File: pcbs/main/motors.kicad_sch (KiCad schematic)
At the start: 49 parts, among them J2 Jumpers, Q1 2SC945, Q2 2SC945, Q3 2SC945, Q4 2SC945, Q5 2SC945, Q6 2SC945, Q7 2SC945, Q8 2SC945

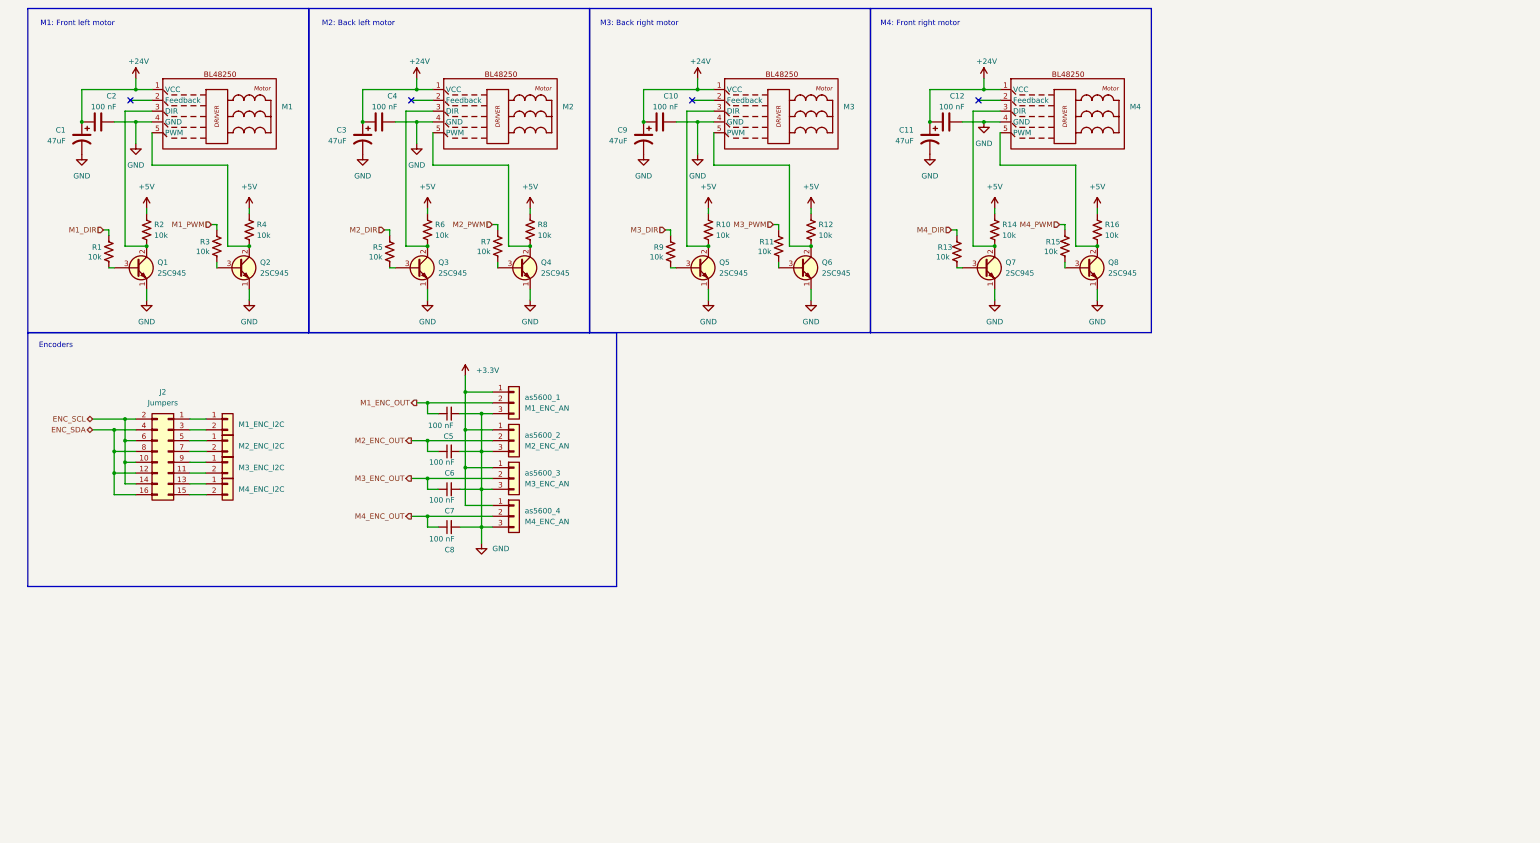
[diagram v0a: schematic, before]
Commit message: Add circuit for motor feedback
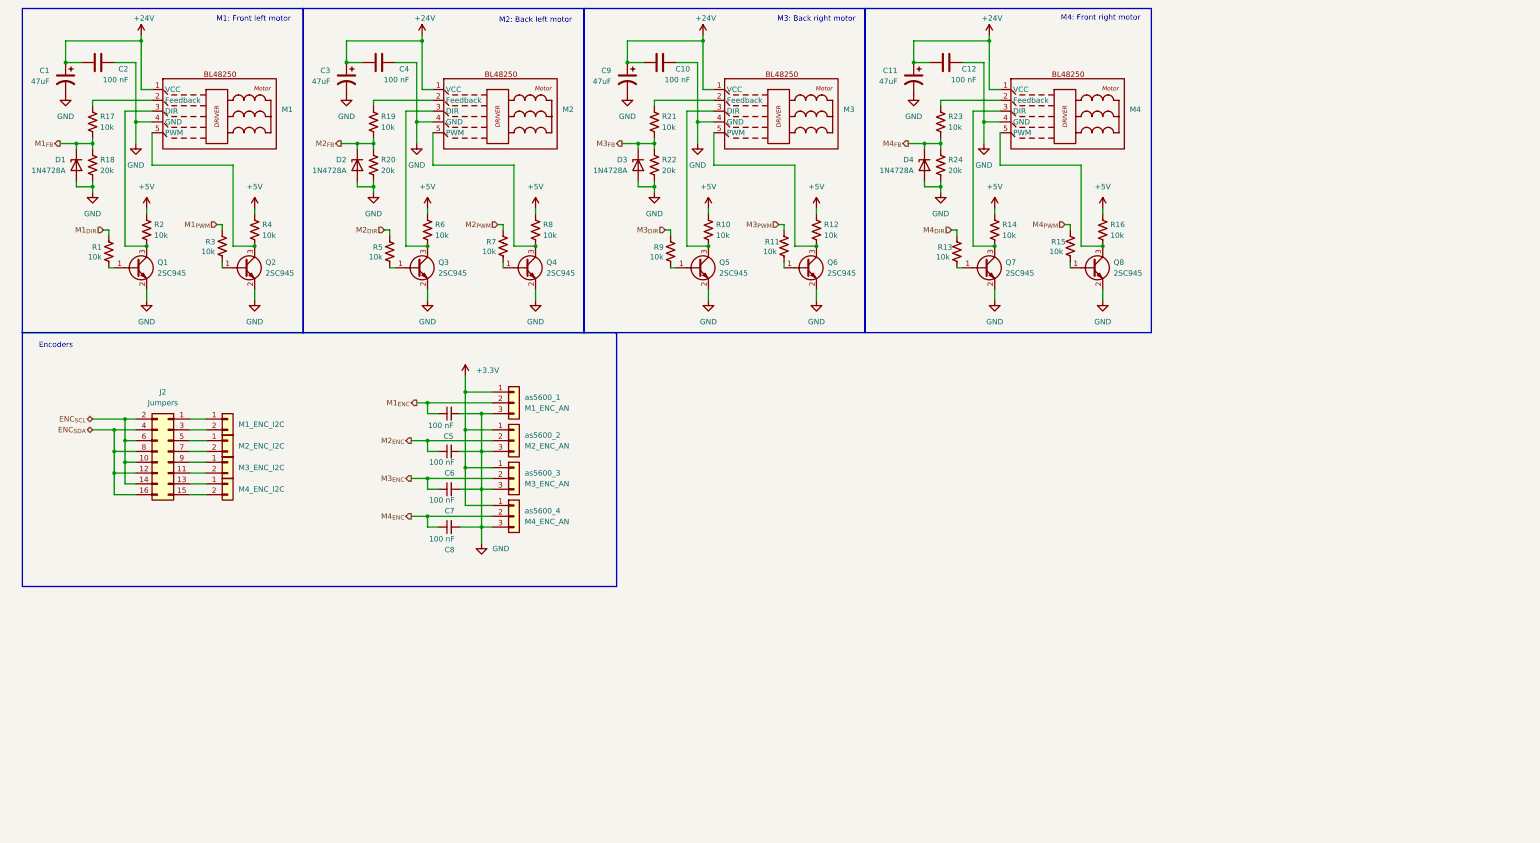
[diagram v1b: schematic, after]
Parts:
- added D1, D2, D3, D4: 1N4728A, Diode_THT:D_DO-41_SOD81_P10.16mm_Horizontal, symbol Diode:1N47xxA
- added R17, R19, R21, R23: 10k, Resistor_THT:R_Axial_DIN0207_L6.3mm_D2.5mm_P7.62mm_Horizontal, symbol Device:R_US
- added R18, R20, R22, R24: 20k, Resistor_THT:R_Axial_DIN0207_L6.3mm_D2.5mm_P7.62mm_Horizontal, symbol Device:R_US
- M1, M2, M3, M4: symbol BL48250:BL48250 -> oxebots:BL48250
- Q1, Q2, Q3, Q4, Q5, Q6, Q7, Q8: footprint Package_TO_SOT_THT:TO-92L_Inline_Wide -> Package_TO_SOT_THT:TO-220-3_Vertical; symbol PCM_Transistor_BJT_AKL:2SC945 -> Transistor_BJT:2SC1945
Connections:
- net GND: now also Q1.2 (E), Q2.2 (E), Q3.2 (E), Q4.2 (E), Q5.2 (E), Q6.2 (E), Q7.2 (E), Q8.2 (E), D1.2 (A), D2.2 (A), D3.2 (A), D4.2 (A), R18.1, R20.1, R22.1, R24.1; no longer Q1.1 (E), Q2.1 (E), Q3.1 (E), Q4.1 (E), Q5.1 (E), Q6.1 (E), Q7.1 (E), Q8.1 (E)
- net at M3.3 (DIR), R10.1: now also Q5.3 (C); no longer Q5.2 (C)
- net at M1.5 (PWM), R4.1: now also Q2.3 (C); no longer Q2.2 (C)
- net at R3.2: now also Q2.1 (B); no longer Q2.3 (B)
- net at M1.3 (DIR), R2.1: now also Q1.3 (C); no longer Q1.2 (C)
- net at R15.2: now also Q8.1 (B); no longer Q8.3 (B)
- net at M2.2 (Feedback): now also R19.2
- net at M2.3 (DIR), R6.1: now also Q3.3 (C); no longer Q3.2 (C)
- net at M2.5 (PWM), R8.1: now also Q4.3 (C); no longer Q4.2 (C)
- net at R13.2: now also Q7.1 (B); no longer Q7.3 (B)
- net at R5.2: now also Q3.1 (B); no longer Q3.3 (B)
- net at R9.2: now also Q5.1 (B); no longer Q5.3 (B)
- net at R11.2: now also Q6.1 (B); no longer Q6.3 (B)
- net at M4.5 (PWM), R16.1: now also Q8.3 (C); no longer Q8.2 (C)
- net at M3.2 (Feedback): now also R21.2
- net at M3.5 (PWM), R12.1: now also Q6.3 (C); no longer Q6.2 (C)
- net at R7.2: now also Q4.1 (B); no longer Q4.3 (B)
- net at M4.3 (DIR), R14.1: now also Q7.3 (C); no longer Q7.2 (C)
- net at M4.2 (Feedback): now also R23.2
- net at R1.2: now also Q1.1 (B); no longer Q1.3 (B)
- net at M1.2 (Feedback): now also R17.2
- net ENC_SCL renamed ENC_{SCL}
- net ENC_SDA renamed ENC_{SDA}
- net M1_DIR renamed M1_{DIR}
- net M1_ENC_OUT renamed M1_{ENC}
- net M1_PWM renamed M1_{PWM}
- net M2_DIR renamed M2_{DIR}
- net M2_ENC_OUT renamed M2_{ENC}
- net M2_PWM renamed M2_{PWM}
- net M3_DIR renamed M3_{DIR}
- net M3_ENC_OUT renamed M3_{ENC}
- net M3_PWM renamed M3_{PWM}
- net M4_DIR renamed M4_{DIR}
- net M4_ENC_OUT renamed M4_{ENC}
- net M4_PWM renamed M4_{PWM}
- new net M1_{FB}: D1.1 (K), R17.1, R18.2
- new net M2_{FB}: D2.1 (K), R19.1, R20.2
- new net M3_{FB}: D3.1 (K), R21.1, R22.2
- new net M4_{FB}: D4.1 (K), R23.1, R24.2
- no-connect marks 4 -> 0
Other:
- moved on the sheet: C1, C2, Q2, Q4, Q6, Q8, R11, R12, R15, R16, R3, R4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

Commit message: Add some probes & update footprints
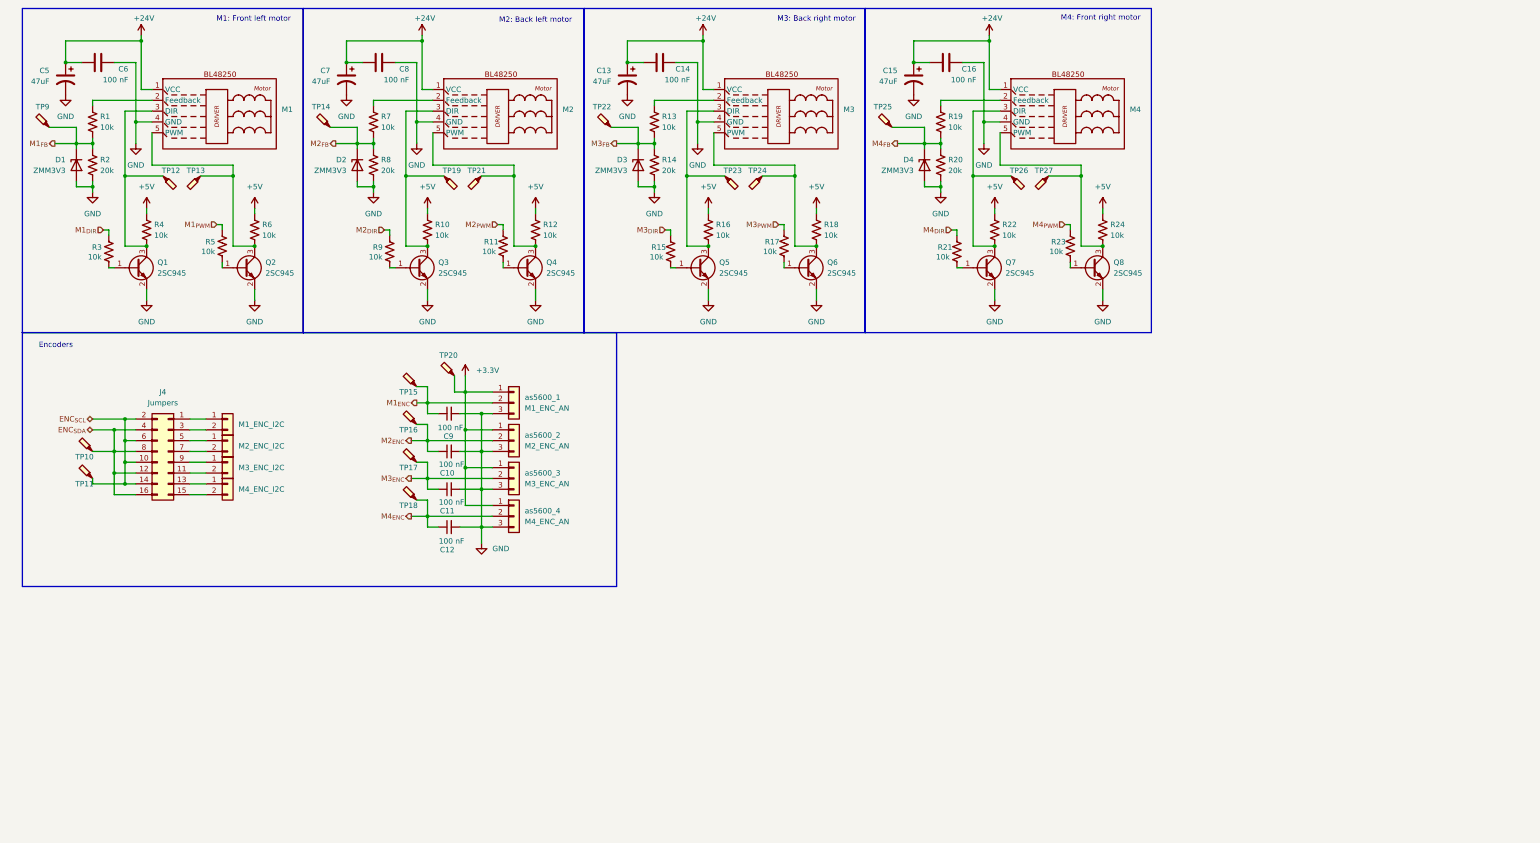
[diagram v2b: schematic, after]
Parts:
- added TP10, TP11, TP17, TP18, TP19, TP21, TP22, TP24, TP25, TP26, TP27: TestPoint_Probe, TestPoint:TestPoint_Pad_D1.0mm, symbol Connector:TestPoint_Probe
- added TP12, TP13, TP14, TP15, TP16, TP20, TP23, TP9: TestPoint_Probe, TestPoint:TestPoint_Loop_D2.50mm_Drill1.0mm_LowProfile, symbol Connector:TestPoint_Probe
- C10: renamed from C6; footprint Capacitor_THT:C_Disc_D5.0mm_W2.5mm_P2.50mm -> Capacitor_SMD:C_0603_1608Metric
- C11: renamed from C7; footprint Capacitor_THT:C_Disc_D5.0mm_W2.5mm_P2.50mm -> Capacitor_SMD:C_0603_1608Metric
- C12: renamed from C8; footprint Capacitor_THT:C_Disc_D5.0mm_W2.5mm_P2.50mm -> Capacitor_SMD:C_0603_1608Metric
- C14: renamed from C10; footprint Capacitor_THT:C_Disc_D5.0mm_W2.5mm_P2.50mm -> Capacitor_SMD:C_0603_1608Metric
- C16: renamed from C12; footprint Capacitor_THT:C_Disc_D5.0mm_W2.5mm_P2.50mm -> Capacitor_SMD:C_0603_1608Metric
- C6: renamed from C2; footprint Capacitor_THT:C_Disc_D5.0mm_W2.5mm_P2.50mm -> Capacitor_SMD:C_0603_1608Metric
- C8: renamed from C4; footprint Capacitor_THT:C_Disc_D5.0mm_W2.5mm_P2.50mm -> Capacitor_SMD:C_0603_1608Metric
- C9: renamed from C5; footprint Capacitor_THT:C_Disc_D5.0mm_W2.5mm_P2.50mm -> Capacitor_SMD:C_0603_1608Metric
- D1, D2, D3, D4: value 1N4728A -> ZMM3V3; footprint Diode_THT:D_DO-41_SOD81_P10.16mm_Horizontal -> Diode_SMD:D_MiniMELF; symbol Diode:1N47xxA -> Diode:ZMMxx
- Q1, Q2, Q3, Q4, Q5, Q6, Q7, Q8: footprint Package_TO_SOT_THT:TO-220-3_Vertical -> Package_TO_SOT_THT:TO-92; symbol Transistor_BJT:2SC1945 -> oxebots:2SC945
- R1: renamed from R17; footprint Resistor_THT:R_Axial_DIN0207_L6.3mm_D2.5mm_P7.62mm_Horizontal -> Resistor_SMD:R_0603_1608Metric
- R10: renamed from R6; footprint Resistor_THT:R_Axial_DIN0207_L6.3mm_D2.5mm_P7.62mm_Horizontal -> Resistor_SMD:R_0603_1608Metric
- R11: renamed from R7; footprint Resistor_THT:R_Axial_DIN0207_L6.3mm_D2.5mm_P7.62mm_Horizontal -> Resistor_SMD:R_0603_1608Metric
- R12: renamed from R8; footprint Resistor_THT:R_Axial_DIN0207_L6.3mm_D2.5mm_P7.62mm_Horizontal -> Resistor_SMD:R_0603_1608Metric
- R13: renamed from R21; footprint Resistor_THT:R_Axial_DIN0207_L6.3mm_D2.5mm_P7.62mm_Horizontal -> Resistor_SMD:R_0603_1608Metric
- R14: renamed from R22; footprint Resistor_THT:R_Axial_DIN0207_L6.3mm_D2.5mm_P7.62mm_Horizontal -> Resistor_SMD:R_0603_1608Metric
- R15: renamed from R9; footprint Resistor_THT:R_Axial_DIN0207_L6.3mm_D2.5mm_P7.62mm_Horizontal -> Resistor_SMD:R_0603_1608Metric
- R16: renamed from R10; footprint Resistor_THT:R_Axial_DIN0207_L6.3mm_D2.5mm_P7.62mm_Horizontal -> Resistor_SMD:R_0603_1608Metric
- R17: renamed from R11; footprint Resistor_THT:R_Axial_DIN0207_L6.3mm_D2.5mm_P7.62mm_Horizontal -> Resistor_SMD:R_0603_1608Metric
- R18: renamed from R12; footprint Resistor_THT:R_Axial_DIN0207_L6.3mm_D2.5mm_P7.62mm_Horizontal -> Resistor_SMD:R_0603_1608Metric
- R19: renamed from R23; footprint Resistor_THT:R_Axial_DIN0207_L6.3mm_D2.5mm_P7.62mm_Horizontal -> Resistor_SMD:R_0603_1608Metric
- R2: renamed from R18; footprint Resistor_THT:R_Axial_DIN0207_L6.3mm_D2.5mm_P7.62mm_Horizontal -> Resistor_SMD:R_0603_1608Metric
- R20: renamed from R24; footprint Resistor_THT:R_Axial_DIN0207_L6.3mm_D2.5mm_P7.62mm_Horizontal -> Resistor_SMD:R_0603_1608Metric
- R21: renamed from R13; footprint Resistor_THT:R_Axial_DIN0207_L6.3mm_D2.5mm_P7.62mm_Horizontal -> Resistor_SMD:R_0603_1608Metric
- R22: renamed from R14; footprint Resistor_THT:R_Axial_DIN0207_L6.3mm_D2.5mm_P7.62mm_Horizontal -> Resistor_SMD:R_0603_1608Metric
- R23: renamed from R15; footprint Resistor_THT:R_Axial_DIN0207_L6.3mm_D2.5mm_P7.62mm_Horizontal -> Resistor_SMD:R_0603_1608Metric
- R24: renamed from R16; footprint Resistor_THT:R_Axial_DIN0207_L6.3mm_D2.5mm_P7.62mm_Horizontal -> Resistor_SMD:R_0603_1608Metric
- R3: renamed from R1; footprint Resistor_THT:R_Axial_DIN0207_L6.3mm_D2.5mm_P7.62mm_Horizontal -> Resistor_SMD:R_0603_1608Metric
- R4: renamed from R2; footprint Resistor_THT:R_Axial_DIN0207_L6.3mm_D2.5mm_P7.62mm_Horizontal -> Resistor_SMD:R_0603_1608Metric
- R5: renamed from R3; footprint Resistor_THT:R_Axial_DIN0207_L6.3mm_D2.5mm_P7.62mm_Horizontal -> Resistor_SMD:R_0603_1608Metric
- R6: renamed from R4; footprint Resistor_THT:R_Axial_DIN0207_L6.3mm_D2.5mm_P7.62mm_Horizontal -> Resistor_SMD:R_0603_1608Metric
- R7: renamed from R19; footprint Resistor_THT:R_Axial_DIN0207_L6.3mm_D2.5mm_P7.62mm_Horizontal -> Resistor_SMD:R_0603_1608Metric
- R8: renamed from R20; footprint Resistor_THT:R_Axial_DIN0207_L6.3mm_D2.5mm_P7.62mm_Horizontal -> Resistor_SMD:R_0603_1608Metric
- R9: renamed from R5; footprint Resistor_THT:R_Axial_DIN0207_L6.3mm_D2.5mm_P7.62mm_Horizontal -> Resistor_SMD:R_0603_1608Metric
- renumbered C9 to C13, C11 to C15, C1 to C5, C3 to C7, J2 to J4
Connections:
- net +3.3V: now also TP20.1
- net ENC_{SCL}: now also TP11.1
- net ENC_{SDA}: now also TP10.1
- net M1_{ENC}: now also TP15.1
- net M1_{FB}: now also TP9.1
- net M2_{ENC}: now also TP16.1
- net M2_{FB}: now also TP14.1
- net M3_{ENC}: now also TP17.1
- net M3_{FB}: now also TP22.1
- net M4_{ENC}: now also TP18.1
- net M4_{FB}: now also TP25.1
- net at M3.3 (DIR), Q5.3 (C), R16.1: now also TP23.1
- net at M1.5 (PWM), Q2.3 (C), R6.1: now also TP13.1
- net at M1.3 (DIR), Q1.3 (C), R4.1: now also TP12.1
- net at M2.3 (DIR), Q3.3 (C), R10.1: now also TP19.1
- net at M2.5 (PWM), Q4.3 (C), R12.1: now also TP21.1
- net at M4.5 (PWM), Q8.3 (C), R24.1: now also TP27.1
- net at M3.5 (PWM), Q6.3 (C), R18.1: now also TP24.1
- net at M4.3 (DIR), Q7.3 (C), R22.1: now also TP26.1

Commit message: Add NRF24 pwr adapter as standalone components
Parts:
- M1: value (none) -> FRONT_LEFT_MOTOR
- M2: value (none) -> BACK_LEFT_MOTOR
- M3: value (none) -> BACK_RIGHT_MOTOR
- M4: value (none) -> FRONT_RIGHT_MOTOR
- TP10: renamed from TP12; value TestPoint_Probe -> M1_DIR_Probe; footprint TestPoint:TestPoint_Loop_D2.50mm_Drill1.0mm_LowProfile -> TestPoint:TestPoint_Pad_D1.0mm
- TP11: renamed from TP13; value TestPoint_Probe -> M1_PWM_Probe
- TP12: renamed from TP14; value TestPoint_Probe -> M2_FB_Probe
- TP13: renamed from TP15; value TestPoint_Probe -> M1_ENC_Probe
- TP14: renamed from TP16; value TestPoint_Probe -> M2_ENC_Probe
- TP15: renamed from TP17; value TestPoint_Probe -> M3_ENC_Probe; footprint TestPoint:TestPoint_Pad_D1.0mm -> TestPoint:TestPoint_Loop_D2.50mm_Drill1.0mm_LowProfile
- TP16: renamed from TP18; value TestPoint_Probe -> M4_ENC_Probe; footprint TestPoint:TestPoint_Pad_D1.0mm -> TestPoint:TestPoint_Loop_D2.50mm_Drill1.0mm_LowProfile
- TP17: renamed from TP19; value TestPoint_Probe -> M2_DIR_Probe
- TP18: renamed from TP20; value TestPoint_Probe -> ENC_VCC_Probe; footprint TestPoint:TestPoint_Loop_D2.50mm_Drill1.0mm_LowProfile -> TestPoint:TestPoint_Pad_D1.0mm
- TP19: renamed from TP21; value TestPoint_Probe -> M2_PWM_Probe; footprint TestPoint:TestPoint_Pad_D1.0mm -> TestPoint:TestPoint_Loop_D2.50mm_Drill1.0mm_LowProfile
- TP20: renamed from TP22; value TestPoint_Probe -> M3_FB_Probe; footprint TestPoint:TestPoint_Pad_D1.0mm -> TestPoint:TestPoint_Loop_D2.50mm_Drill1.0mm_LowProfile
- TP21: renamed from TP23; value TestPoint_Probe -> M3_DIR_Probe; footprint TestPoint:TestPoint_Loop_D2.50mm_Drill1.0mm_LowProfile -> TestPoint:TestPoint_Pad_D1.0mm
- TP22: renamed from TP24; value TestPoint_Probe -> M3_PWM_Probe; footprint TestPoint:TestPoint_Pad_D1.0mm -> TestPoint:TestPoint_Loop_D2.50mm_Drill1.0mm_LowProfile
- TP23: renamed from TP25; value TestPoint_Probe -> M4_FB_Probe; footprint TestPoint:TestPoint_Pad_D1.0mm -> TestPoint:TestPoint_Loop_D2.50mm_Drill1.0mm_LowProfile
- TP24: renamed from TP26; value TestPoint_Probe -> M4_DIR_Probe
- TP25: renamed from TP27; value TestPoint_Probe -> M4_PWM_Probe; footprint TestPoint:TestPoint_Pad_D1.0mm -> TestPoint:TestPoint_Loop_D2.50mm_Drill1.0mm_LowProfile
- TP7: renamed from TP9; value TestPoint_Probe -> M1_FB_Probe
- TP8: renamed from TP10; value TestPoint_Probe -> ENC_SDA_Probe; footprint TestPoint:TestPoint_Pad_D1.0mm -> TestPoint:TestPoint_Loop_D2.50mm_Drill1.0mm_LowProfile
- TP9: renamed from TP11; value TestPoint_Probe -> ENC_SCL_Probe; footprint TestPoint:TestPoint_Pad_D1.0mm -> TestPoint:TestPoint_Loop_D2.50mm_Drill1.0mm_LowProfile
- renumbered C7 to C10, C8 to C11, C9 to C12, C10 to C13, C11 to C14, C12 to C15, C13 to C16, C14 to C17, C15 to C18, C16 to C19, C5 to C8, C6 to C9
